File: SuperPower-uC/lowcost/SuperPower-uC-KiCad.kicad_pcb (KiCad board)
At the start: 2 copper layers, 81 x 28.5 mm, 84 parts, among them J1 Battery connector, J2 Thermistor, J3 USB_B_Micro, J4 Solar in, J5 main pin header fight, J6 main pin header left, Q1 2N7002, Q2 2N7002, Q3 S8050, Q4 S8050, Q5 AO3401A, Q6 AO3401A, Q7 2N7002, U1 FS312F-G, U10 FP6291LR, U11 ME6210A33P, U12 ME6210A33P, U13 ESP32-WROOM32, U2 FS8205A, U3 LC709203FQH, U4 TP4056, U5 CH340G, U6 AMS1117-3.3, U7 PCF8563T, U8 XC6206P332MR, U9 TCA6408A, Y1 12MHZ, Y2 32.768KHz

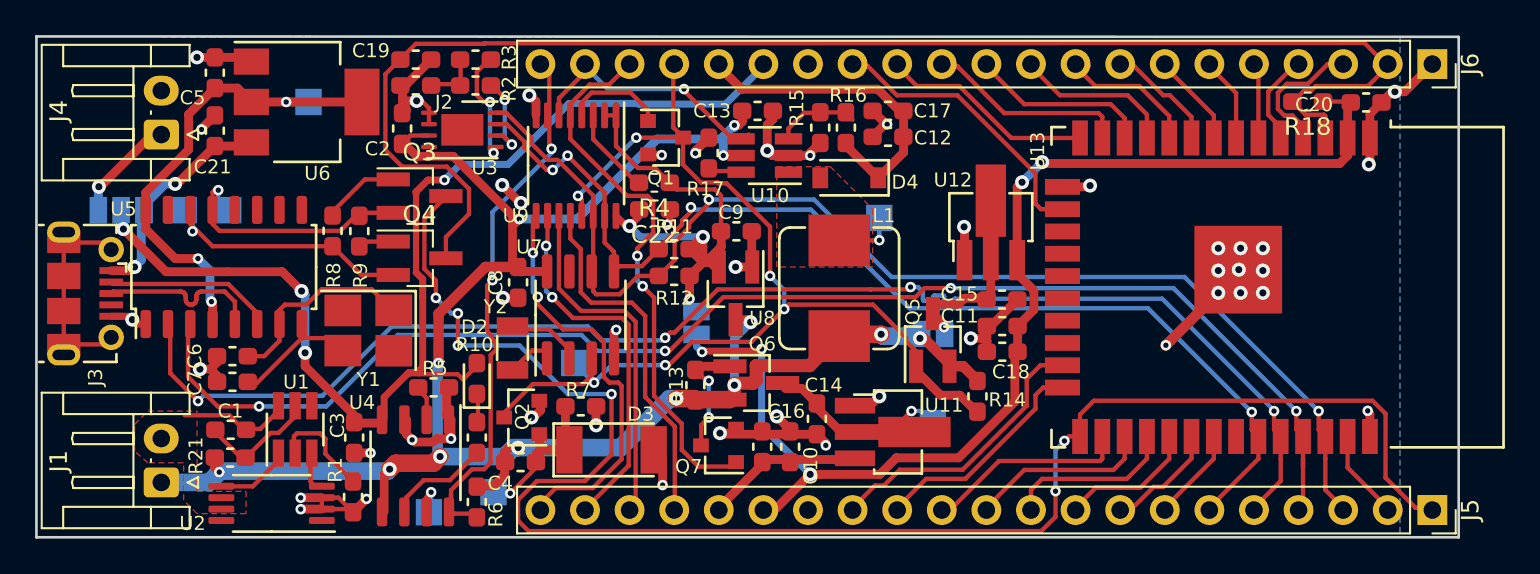
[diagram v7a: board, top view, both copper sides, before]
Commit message: added proper high side cutoff for 5v regulator
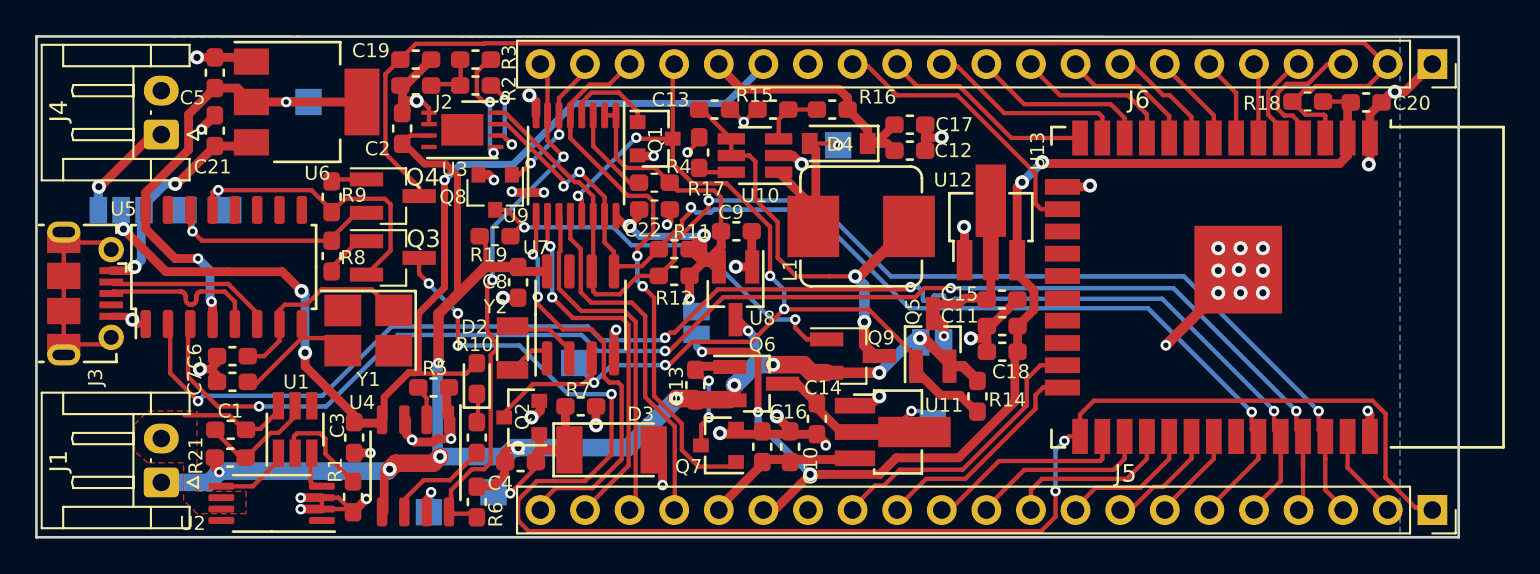
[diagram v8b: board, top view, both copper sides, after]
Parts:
- added Q8: 2N7002, Package_TO_SOT_SMD:SOT-23, F.Cu at (128.1, 103.8)
- added Q9: AO3401A, Package_TO_SOT_SMD:SOT-23_Handsoldering, F.Cu at (148.5, 113.1)
- added R19: 180k, Resistor_SMD:R_0603_1608Metric_Pad1.05x0.95mm_HandSolder, F.Cu at (128.1, 106.3)
- C19: value 0.1µF -> 1µF
- R18: value 180k -> 10k
- moved TP5 4.75 mm to (147.7, 101.1)
- moved Q4 3.85 mm to (122.3, 104.0)
- moved Q3 3.84 mm to (122.3, 107.6)
- moved L1 3.74 mm to (149.0, 105.8), turned to 180 degrees
- moved R15 2.88 mm to (143.9, 99.1), turned to 180 degrees
- moved R9 2.51 mm to (118.8, 104.1), turned to 270 degrees
- moved C13 2.45 mm to (140.6, 99.1)
- moved D4 2.04 mm to (147.7, 101.0)
- moved C17 1.47 mm to (151.7, 100.0), turned to 0 degrees
- moved C12 1.47 mm to (151.7, 101.4), turned to 0 degrees
- moved R8 1.43 mm to (118.8, 107.5), turned to 90 degrees
- moved R16 1.29 mm to (147.3, 99.1), turned to 180 degrees
- moved Q1 0.59 mm to (137.2, 100.8)
- moved U10 0.56 mm to (142.9, 101.7)
- moved R17 0.55 mm to (139.7, 101.6)
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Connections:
- C13 pad 1: /Battery Module/VBAT -> Net-(C13-Pad1)
- L1 pad 1: /Battery Module/VBAT -> Net-(C13-Pad1)
- U10 pad 4: 5V_EN -> Net-(C13-Pad1)
- U10 pad 5: /Battery Module/VBAT -> Net-(C13-Pad1)
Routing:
- net Net-(C13-Pad1): track 0.00 -> 25.3 mm, vias 0 -> 2
- net Net-(Q8-Pad3): track 0.00 -> 23.2 mm, vias 0 -> 2
- net /Battery Module/VBAT: track 110.8 -> 92.1 mm, vias 13 -> 11
- net /Charger I/O/RST: track 84.1 -> 77.3 mm
- net 5V_EN: track 14.4 -> 8.08 mm, vias 1 -> 2
- net Net-(D4-Pad2): track 5.22 -> 10.5 mm
- net /Charger I/O/GPIO0: track 93.9 -> 89.8 mm
- net /MCU Module/5V: track 18.7 -> 14.8 mm
- net Net-(Q3-Pad2): track 14.4 -> 18.1 mm
- net /Charger I/O/VCHARGE: track 64.6 -> 62.9 mm
- net Net-(Q4-Pad2): track 15.3 -> 13.6 mm
- net Net-(Q3-Pad1): track 4.43 -> 2.83 mm
- net Net-(R15-Pad1): track 4.80 -> 3.52 mm
- net INT_IO: track 62.6 -> 61.7 mm
- net GND: track 89.2 -> 88.6 mm, vias 46 -> 47
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- removed copper zone on F.Cu, net Net-(D4-Pad2)
